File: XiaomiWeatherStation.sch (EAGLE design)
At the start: 12 parts, among them J1 1X2-3.5MM, K1 RELAY-SPDT

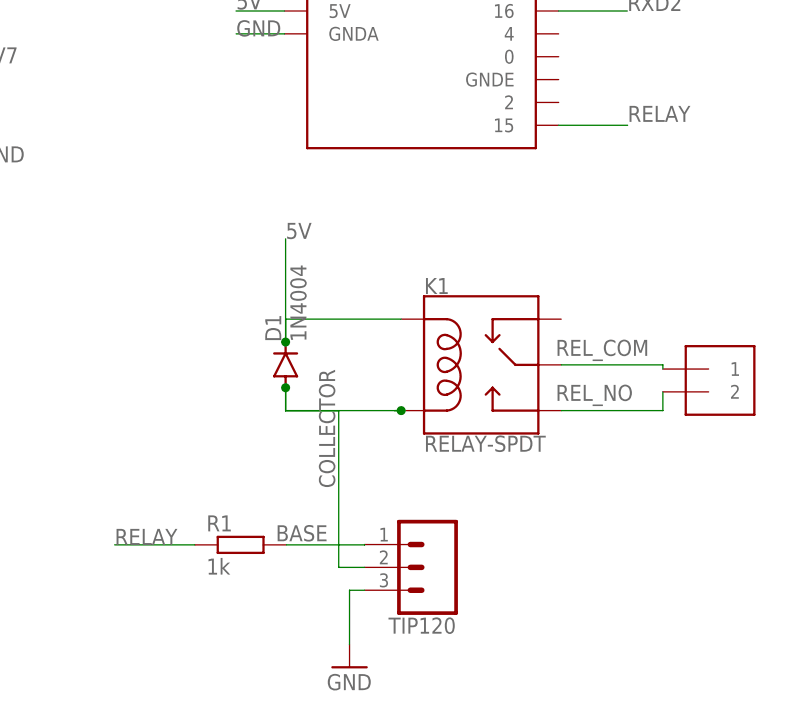
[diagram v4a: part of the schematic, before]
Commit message: Adds 3d packages to the components
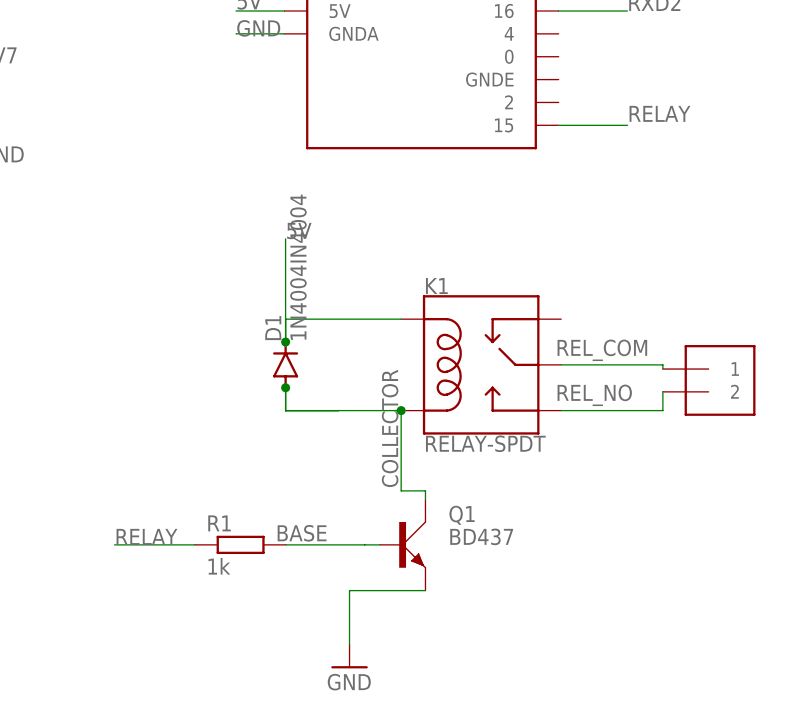
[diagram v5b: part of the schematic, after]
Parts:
- removed TIP120: (no value), SparkFun-Connectors:CONN_03LONGPADS
- added Q1: BD437, transistor-power:BD437
- D1: value 1N4004 -> 1N4004IN4004; device diode:1N4004 -> diode:1N4004IN4004
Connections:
- net BASE: now also Q1.B; no longer TIP120.1
- net COLLECTOR: now also Q1.C; no longer TIP120.2
- net GND: now also Q1.E; no longer TIP120.3
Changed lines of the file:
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@@
 <setting verticaltext="up"/>
 </settings>
-<grid distance="1" unitdist="mm" unit="mm" style="dots" multiple="1" display="yes" altdistance="0.1" altunitdist="mm" altunit="mm"/>
+<grid distance="1" unitdist="mm" unit="mm" style="lines" multiple="1" display="no" altdistance="0.01" altunitdist="inch" altunit="inch"/>
 <layers>
 <layer number="1" name="Top" color="4" fill="1" visible="no" active="no"/>
@@
 <layer number="250" name="Descript" color="7" fill="1" visible="no" active="no"/>
 <layer number="251" name="SMDround" color="7" fill="1" visible="no" active="no"/>
+<layer number="253" name="Extra" color="7" fill="1" visible="no" active="no"/>
 <layer number="254" name="cooling" color="7" fill="1" visible="no" active="yes"/>
 <layer number="255" name="255bmp" color="1" fill="10" visible="no" active="yes"/>
@@
 </classes>
 <parts>
-<part name="IC1" library="SSFD - ESP32 WEMOS LOLIN CHINA W_BATT" deviceset="SSFD_LOLIN32_WEMOS_CHINA_W_BATT" device=""/>
-<part name="U$1" library="SIM800LMODULE" deviceset="SIM800LMODULE" device=""/>
+<part name="IC1" library="SSFD - ESP32 WEMOS LOLIN CHINA W_BATT" library_urn="urn:adsk.eagle:library:31562966" deviceset="SSFD_LOLIN32_WEMOS_CHINA_W_BATT" device="" package3d_urn="urn:adsk.eagle:package:31562973/2"/>
+<part name="U$1" library="SIM800LMODULE" library_urn="urn:adsk.eagle:library:31562961" deviceset="SIM800LMODULE" device="" package3d_urn="urn:adsk.eagle:package:31562964/4"/>
 <part name="LCD" library="pinhead" library_urn="urn:adsk.eagle:library:325" deviceset="PINHD-1X4" device="" package3d_urn="urn:adsk.eagle:package:22407/2"/>
 <part name="DS3231" library="pinhead" library_urn="urn:adsk.eagle:library:325" deviceset="PINHD-1X4" device="" package3d_urn="urn:adsk.eagle:package:22407/2"/>
-<part name="U$3" library="diy-modules" deviceset="DC-DC-STEP-DOWN-LM2596" device=""/>
+<part name="U$3" library="diy-modules" library_urn="urn:adsk.eagle:library:31562516" deviceset="DC-DC-STEP-DOWN-LM2596" device="" package3d_urn="urn:adsk.eagle:package:31562766/2"/>
 <part name="JP3" library="pinhead" library_urn="urn:adsk.eagle:library:325" deviceset="PINHD-1X2" device="" package3d_urn="urn:adsk.eagle:package:22435/2"/>
 <part name="FRAME1" library="frames" library_urn="urn:adsk.eagle:library:229" deviceset="A3L-LOC" device=""/>
 <part name="R1" library="rcl" library_urn="urn:adsk.eagle:library:334" deviceset="R-EU_" device="0204/7" package3d_urn="urn:adsk.eagle:package:23498/2" value="1k"/>
-<part name="D1" library="diode" library_urn="urn:adsk.eagle:library:210" deviceset="1N4004" device="" package3d_urn="urn:adsk.eagle:package:43336/1"/>
-<part name="K1" library="SparkFun-Electromechanical" deviceset="RELAY-SPDT" device=""/>
-<part name="J1" library="adafruit" deviceset="1X2" device="-3.5MM"/>
+<part name="D1" library="diode" library_urn="urn:adsk.eagle:library:31568414" deviceset="1N4004" device="IN4004" package3d_urn="urn:adsk.eagle:package:31568383/1"/>
+<part name="K1" library="SparkFun-Electromechanical" library_urn="urn:adsk.eagle:library:31566981" deviceset="RELAY-SPDT" device="" package3d_urn="urn:adsk.eagle:package:31567014/2"/>
+<part name="J1" library="adafruit" library_urn="urn:adsk.eagle:library:31565267" deviceset="1X2" device="-3.5MM" package3d_urn="urn:adsk.eagle:package:31566436/3"/>
 <part name="GND1" library="supply1" library_urn="urn:adsk.eagle:library:371" deviceset="GND" device=""/>
-<part name="SD_CARD" library="SparkFun-Connectors" deviceset="CONN_06" device="LONGPADS"/>
-<part name="TIP120" library="SparkFun-Connectors" deviceset="CONN_03" device="LONGPADS"/>
+<part name="SD_CARD" library="SparkFun-Connectors" library_urn="urn:adsk.eagle:library:31567038" deviceset="CONN_06" device="LONGPADS" package3d_urn="urn:adsk.eagle:package:31567581/1"/>
+<part name="Q1" library="transistor-power" library_urn="urn:adsk.eagle:library:31570476" deviceset="BD437" device="" package3d_urn="urn:adsk.eagle:package:31570603/2"/>
 </parts>
 <sheets>
@@
 <attribute name="NAME" x="241.92" y="129.668" size="1.778" layer="95" font="vector"/>
 </instance>
-<instance part="TIP120" gate="J$1" x="193.4" y="55.5" smashed="yes" rot="R180">
-<attribute name="VALUE" x="195.94" y="62.866" size="1.778" layer="96" font="vector" rot="R180"/>
-<attribute name="NAME" x="195.94" y="49.912" size="1.778" layer="95" font="vector" rot="R180"/>
+<instance part="Q1" gate="1" x="190" y="58" smashed="yes">
+<attribute name="NAME" x="195.08" y="60.54" size="1.778" layer="95"/>
+<attribute name="VALUE" x="195.08" y="58" size="1.778" layer="96"/>
 </instance>
 </instances>
@@
 </segment>
 <segment>
-<pinref part="GND1" gate="1" pin="GND"/>
-<pinref part="TIP120" gate="J$1" pin="3"/>
-<wire x1="184.1" y1="46.94" x2="184.1" y2="52.96" width="0.1524" layer="91"/>
-<wire x1="184.1" y1="52.96" x2="185.78" y2="52.96" width="0.1524" layer="91"/>
-</segment>
-<segment>
 <pinref part="SD_CARD" gate="G$1" pin="1"/>
 <wire x1="252.08" y1="113.92" x2="262" y2="113.92" width="0.1524" layer="91"/>
 <label x="262" y="114" size="1.778" layer="95"/>
+</segment>
+<segment>
+<pinref part="GND1" gate="1" pin="GND"/>
+<pinref part="Q1" gate="1" pin="E"/>
+<wire x1="184.1" y1="46.94" x2="184.1" y2="52.92" width="0.1524" layer="91"/>
+<wire x1="184.1" y1="52.92" x2="192.54" y2="52.92" width="0.1524" layer="91"/>
 </segment>
 </net>
@@
 <wire x1="177" y1="72.92" x2="189.84" y2="72.92" width="0.1524" layer="91"/>
 <junction x="189.84" y="72.92"/>
-<pinref part="TIP120" gate="J$1" pin="2"/>
-<wire x1="185.78" y1="55.5" x2="182.9" y2="55.5" width="0.1524" layer="91"/>
-<wire x1="182.9" y1="55.5" x2="182.9" y2="72.9" width="0.1524" layer="91"/>
 <wire x1="182.9" y1="72.9" x2="177" y2="72.9" width="0.1524" layer="91"/>
 <wire x1="177" y1="72.9" x2="177" y2="75.46" width="0.1524" layer="91"/>
 <junction x="177" y="75.46"/>
-<label x="182.5" y="64.3" size="1.778" layer="95" rot="R90"/>
+<label x="189.5" y="64.3" size="1.778" layer="95" rot="R90"/>
+<pinref part="Q1" gate="1" pin="C"/>
+<wire x1="192.54" y1="63.08" x2="192.54" y2="64" width="0.1524" layer="91"/>
+<wire x1="192.54" y1="64" x2="189.84" y2="64" width="0.1524" layer="91"/>
+<wire x1="189.84" y1="64" x2="189.84" y2="72.92" width="0.1524" layer="91"/>
 </segment>
 </net>
@@
 <segment>
 <pinref part="R1" gate="G$1" pin="2"/>
-<pinref part="TIP120" gate="J$1" pin="1"/>
-<wire x1="177.08" y1="58" x2="185.78" y2="58" width="0.1524" layer="91"/>
+<label x="175.9" y="58.4" size="1.778" layer="95"/>
+<pinref part="Q1" gate="1" pin="B"/>
+<wire x1="187.46" y1="58" x2="177.08" y2="58" width="0.1524" layer="91"/>
+</segment>
+</net>
+<net name="N$1" class="0">
+<segment>
 <wire x1="185.78" y1="58" x2="185.78" y2="58.04" width="0.1524" layer="91"/>
-<label x="175.9" y="58.4" size="1.778" layer="95"/>
-</segment>
-</net>
+</segment>
+</net>

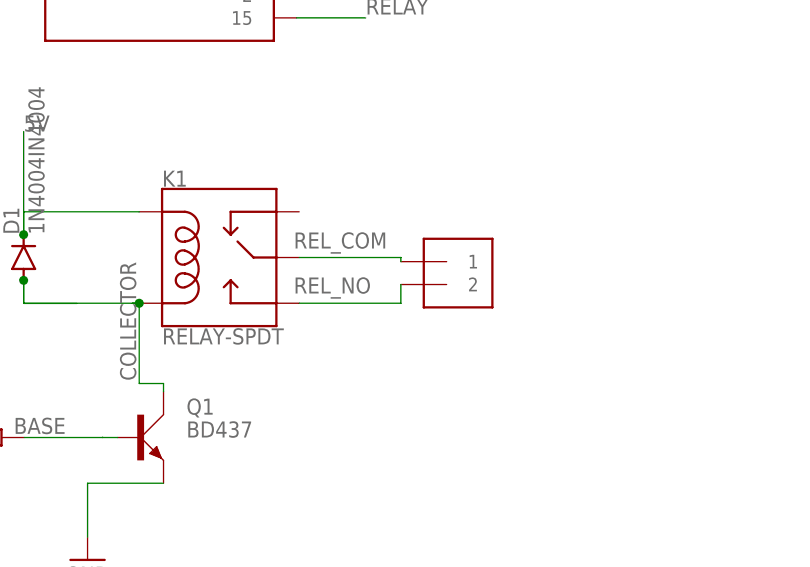
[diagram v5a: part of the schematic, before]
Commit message: Changes the terminal block from 3.5mm to 5mm
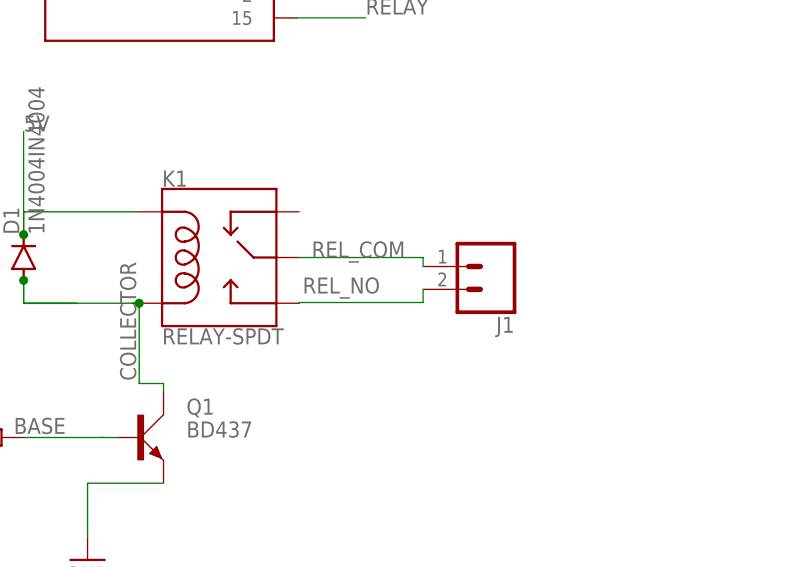
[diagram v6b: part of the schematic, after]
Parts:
- J1: value 1X2-3.5MM -> (none); device adafruit:1X2-3.5MM -> SparkFun-Connectors:CONN_025MM
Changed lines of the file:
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@@
 <part name="D1" library="diode" library_urn="urn:adsk.eagle:library:31568414" deviceset="1N4004" device="IN4004" package3d_urn="urn:adsk.eagle:package:31568383/1"/>
 <part name="K1" library="SparkFun-Electromechanical" library_urn="urn:adsk.eagle:library:31566981" deviceset="RELAY-SPDT" device="" package3d_urn="urn:adsk.eagle:package:31567014/2"/>
-<part name="J1" library="adafruit" library_urn="urn:adsk.eagle:library:31565267" deviceset="1X2" device="-3.5MM" package3d_urn="urn:adsk.eagle:package:31566436/3"/>
 <part name="GND1" library="supply1" library_urn="urn:adsk.eagle:library:371" deviceset="GND" device=""/>
 <part name="SD_CARD" library="SparkFun-Connectors" library_urn="urn:adsk.eagle:library:31567038" deviceset="CONN_06" device="LONGPADS" package3d_urn="urn:adsk.eagle:package:31567581/1"/>
 <part name="Q1" library="transistor-power" library_urn="urn:adsk.eagle:library:31570476" deviceset="BD437" device="" package3d_urn="urn:adsk.eagle:package:31570603/2"/>
+<part name="J1" library="SparkFun-Connectors" library_urn="urn:adsk.eagle:library:31567038" deviceset="CONN_02" device="5MM" package3d_urn="urn:adsk.eagle:package:31567599/1"/>
 </parts>
 <sheets>
@@
 <attribute name="VALUE" x="192.38" y="68.348" size="1.778" layer="96" font="vector"/>
 </instance>
-<instance part="J1" gate="G$1" x="224" y="75" smashed="yes"/>
 <instance part="GND1" gate="1" x="184.1" y="44.4" smashed="yes">
 <attribute name="VALUE" x="181.56" y="41.86" size="1.778" layer="96"/>
@@
 <attribute name="NAME" x="195.08" y="60.54" size="1.778" layer="95"/>
 <attribute name="VALUE" x="195.08" y="58" size="1.778" layer="96"/>
+</instance>
+<instance part="J1" gate="G$1" x="229" y="77" smashed="yes" rot="R180">
+<attribute name="VALUE" x="231.54" y="81.826" size="1.778" layer="96" font="vector" rot="R180"/>
+<attribute name="NAME" x="231.54" y="71.412" size="1.778" layer="95" font="vector" rot="R180"/>
 </instance>
 </instances>
@@
 </segment>
 </net>
-<net name="REL_COM" class="0">
-<segment>
-<pinref part="K1" gate="K$1" pin="MAIN"/>
-<pinref part="J1" gate="G$1" pin="1"/>
-<wire x1="207.62" y1="78" x2="218.92" y2="78" width="0.1524" layer="91"/>
-<wire x1="218.92" y1="78" x2="218.92" y2="77.54" width="0.1524" layer="91"/>
-<label x="207" y="79" size="1.778" layer="95"/>
-</segment>
-</net>
-<net name="REL_NO" class="0">
-<segment>
-<pinref part="K1" gate="K$1" pin="NO"/>
-<pinref part="J1" gate="G$1" pin="2"/>
-<wire x1="207.62" y1="72.92" x2="218.92" y2="72.92" width="0.1524" layer="91"/>
-<wire x1="218.92" y1="72.92" x2="218.92" y2="75" width="0.1524" layer="91"/>
-<label x="207" y="74" size="1.778" layer="95"/>
-</segment>
-</net>
 <net name="RELAY" class="0">
 <segment>
@@
 </segment>
 </net>
+<net name="REL_NO" class="0">
+<segment>
+<pinref part="K1" gate="K$1" pin="NO"/>
+<wire x1="207.62" y1="72.92" x2="207.62" y2="73" width="0.1524" layer="91"/>
+<wire x1="207.62" y1="73" x2="221.38" y2="73" width="0.1524" layer="91"/>
+<label x="208" y="74" size="1.778" layer="95"/>
+<pinref part="J1" gate="G$1" pin="2"/>
+<wire x1="221.38" y1="74.46" x2="221.38" y2="73" width="0.1524" layer="91"/>
+</segment>
+</net>
+<net name="REL_COM" class="0">
+<segment>
+<pinref part="K1" gate="K$1" pin="MAIN"/>
+<pinref part="J1" gate="G$1" pin="1"/>
+<wire x1="207.62" y1="78" x2="221.38" y2="78" width="0.1524" layer="91"/>
+<wire x1="221.38" y1="78" x2="221.38" y2="77" width="0.1524" layer="91"/>
+<label x="209" y="78" size="1.778" layer="95"/>
+</segment>
+</net>
